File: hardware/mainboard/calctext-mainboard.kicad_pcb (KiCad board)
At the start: 4 copper layers, 65 x 97.8 mm, 9 parts, among them J1 Conn_ARM_SWD_TagConnect_TC203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

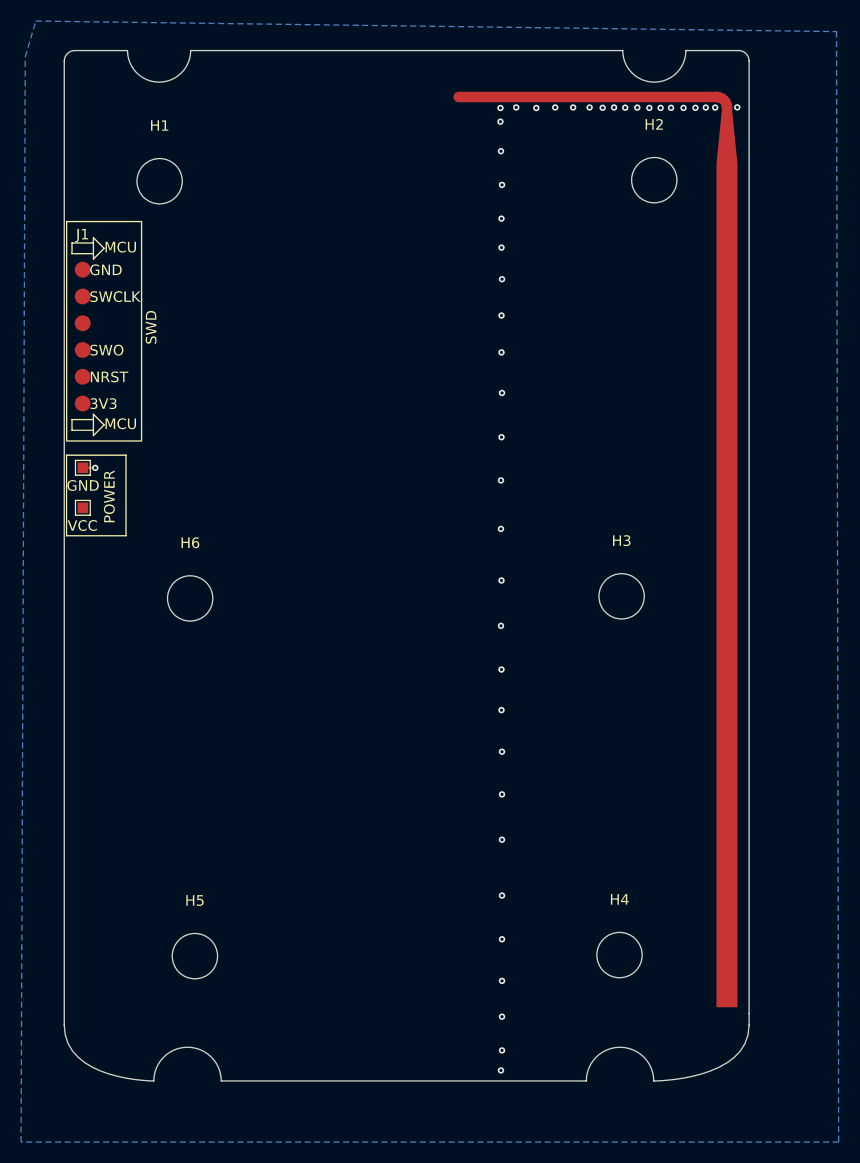
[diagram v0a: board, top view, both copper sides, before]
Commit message: Lay out calculator keypad contacts
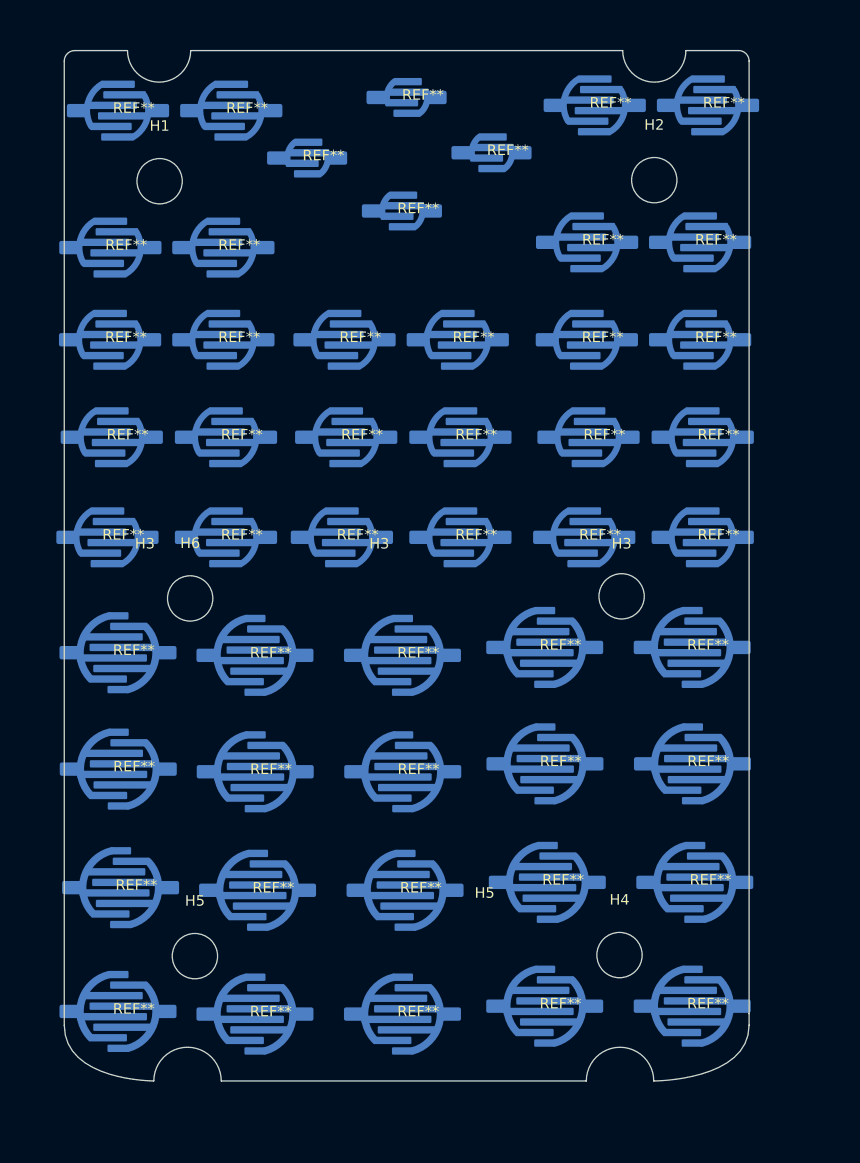
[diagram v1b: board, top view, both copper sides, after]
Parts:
- removed J1: Conn_ARM_SWD_TagConnect_TC2030-NL, STLINKV2:STLINKV2
- removed TP2: +4.2V, TestPoint:TestPoint_Pad_1.0x1.0mm
- removed TP3: GND, TestPoint:TestPoint_Pad_1.0x1.0mm
- added REF**: keypad_trace_button_medium, CalcText:keypad_trace_button_medium, F.Cu at (21.3, 35.5)
- added REF**: keypad_trace_button_medium, CalcText:keypad_trace_button_medium, F.Cu at (66.5, 44.2)
- added REF**: keypad_trace_button_large, CalcText:keypad_trace_button_large, F.Cu at (62.5, 107.5)
- added REF**: keypad_trace_button_small, CalcText:keypad_trace_button_small, F.Cu at (49.4, 21.2)
- added REF**: keypad_trace_button_small, CalcText:keypad_trace_button_small, F.Cu at (49.0, 32.0)
- added REF**: keypad_trace_button_medium, CalcText:keypad_trace_button_medium, F.Cu at (66.7, 53.5)
- added REF**: keypad_trace_button_large, CalcText:keypad_trace_button_large, F.Cu at (35.0, 108.2)
- added REF**: keypad_trace_button_medium, CalcText:keypad_trace_button_medium, F.Cu at (22.0, 22.5)
- added REF**: keypad_trace_button_medium, CalcText:keypad_trace_button_medium, F.Cu at (78.0, 22.0)
- added REF**: keypad_trace_button_large, CalcText:keypad_trace_button_large, F.Cu at (49.2, 96.5)
- added REF**: keypad_trace_button_large, CalcText:keypad_trace_button_large, F.Cu at (22.2, 96.2)
- added REF**: keypad_trace_button_large, CalcText:keypad_trace_button_large, F.Cu at (76.7, 95.8)
- added REF**: keypad_trace_button_large, CalcText:keypad_trace_button_large, F.Cu at (35.2, 96.5)
- added REF**: keypad_trace_button_medium, CalcText:keypad_trace_button_medium, F.Cu at (32.0, 35.5)
- added REF**: keypad_trace_button_large, CalcText:keypad_trace_button_large, F.Cu at (22.0, 74.0)
- added REF**: keypad_trace_button_medium, CalcText:keypad_trace_button_medium, F.Cu at (43.7, 53.5)
- added REF**: keypad_trace_button_medium, CalcText:keypad_trace_button_medium, F.Cu at (43.2, 63.0)
- added REF**: keypad_trace_button_large, CalcText:keypad_trace_button_large, F.Cu at (76.5, 84.5)
- added REF**: keypad_trace_button_large, CalcText:keypad_trace_button_large, F.Cu at (49.0, 85.2)
- added REF**: keypad_trace_button_large, CalcText:keypad_trace_button_large, F.Cu at (62.5, 84.5)
- added REF**: keypad_trace_button_large, CalcText:keypad_trace_button_large, F.Cu at (22.0, 108.0)
- added REF**: keypad_trace_button_medium, CalcText:keypad_trace_button_medium, F.Cu at (77.2, 44.2)
- added REF**: keypad_trace_button_medium, CalcText:keypad_trace_button_medium, F.Cu at (54.5, 53.5)
- added REF**: keypad_trace_button_medium, CalcText:keypad_trace_button_medium, F.Cu at (77.2, 35.0)
- added REF**: keypad_trace_button_medium, CalcText:keypad_trace_button_medium, F.Cu at (21.2, 44.2)
- added REF**: keypad_trace_button_large, CalcText:keypad_trace_button_large, F.Cu at (76.5, 73.5)
- added REF**: keypad_trace_button_medium, CalcText:keypad_trace_button_medium, F.Cu at (43.5, 44.2)
- added REF**: keypad_trace_button_medium, CalcText:keypad_trace_button_medium, F.Cu at (54.5, 63.0)
- added REF**: keypad_trace_button_medium, CalcText:keypad_trace_button_medium, F.Cu at (77.5, 53.5)
- added REF**: keypad_trace_button_medium, CalcText:keypad_trace_button_medium, F.Cu at (66.2, 63.0)
- added REF**: keypad_trace_button_large, CalcText:keypad_trace_button_large, F.Cu at (35.0, 74.2)
- added REF**: keypad_trace_button_large, CalcText:keypad_trace_button_large, F.Cu at (62.7, 95.8)
- added REF**: keypad_trace_button_medium, CalcText:keypad_trace_button_medium, F.Cu at (67.2, 22.0)
- added REF**: keypad_trace_button_medium, CalcText:keypad_trace_button_medium, F.Cu at (54.2, 44.2)
- added REF**: keypad_trace_button_medium, CalcText:keypad_trace_button_medium, F.Cu at (21.0, 63.0)
- added REF**: keypad_trace_button_medium, CalcText:keypad_trace_button_medium, F.Cu at (21.4, 53.5)
- added REF**: keypad_trace_button_small, CalcText:keypad_trace_button_small, F.Cu at (40.0, 27.0)
- added REF**: keypad_trace_button_large, CalcText:keypad_trace_button_large, F.Cu at (22.0, 85.0)
- added REF**: keypad_trace_button_medium, CalcText:keypad_trace_button_medium, F.Cu at (77.5, 63.0)
- added REF**: keypad_trace_button_medium, CalcText:keypad_trace_button_medium, F.Cu at (32.2, 63.0)
- added REF**: keypad_trace_button_medium, CalcText:keypad_trace_button_medium, F.Cu at (66.5, 35.0)
- added REF**: keypad_trace_button_large, CalcText:keypad_trace_button_large, F.Cu at (62.5, 73.5)
- added REF**: keypad_trace_button_medium, CalcText:keypad_trace_button_medium, F.Cu at (32.8, 22.5)
- added REF**: keypad_trace_button_large, CalcText:keypad_trace_button_large, F.Cu at (49.0, 108.2)
- added REF**: keypad_trace_button_large, CalcText:keypad_trace_button_large, F.Cu at (76.5, 107.5)
- added REF**: keypad_trace_button_medium, CalcText:keypad_trace_button_medium, F.Cu at (32.0, 44.2)
- added REF**: keypad_trace_button_large, CalcText:keypad_trace_button_large, F.Cu at (49.0, 74.2)
- added REF**: keypad_trace_button_large, CalcText:keypad_trace_button_large, F.Cu at (35.0, 85.2)
- added REF**: keypad_trace_button_medium, CalcText:keypad_trace_button_medium, F.Cu at (32.2, 53.5)
- added REF**: keypad_trace_button_small, CalcText:keypad_trace_button_small, F.Cu at (57.5, 26.5)
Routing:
- net (no net): track 26.3 -> 0.00 mm
- net GND: track 1.18 -> 0.00 mm, vias 44 -> 0
- removed copper zone on B.Cu, net GND
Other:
- board text added: "H3"
- board text added: "H5"
- board text removed: "GND"
- board text removed: "POWER"
- board text removed: "VCC"

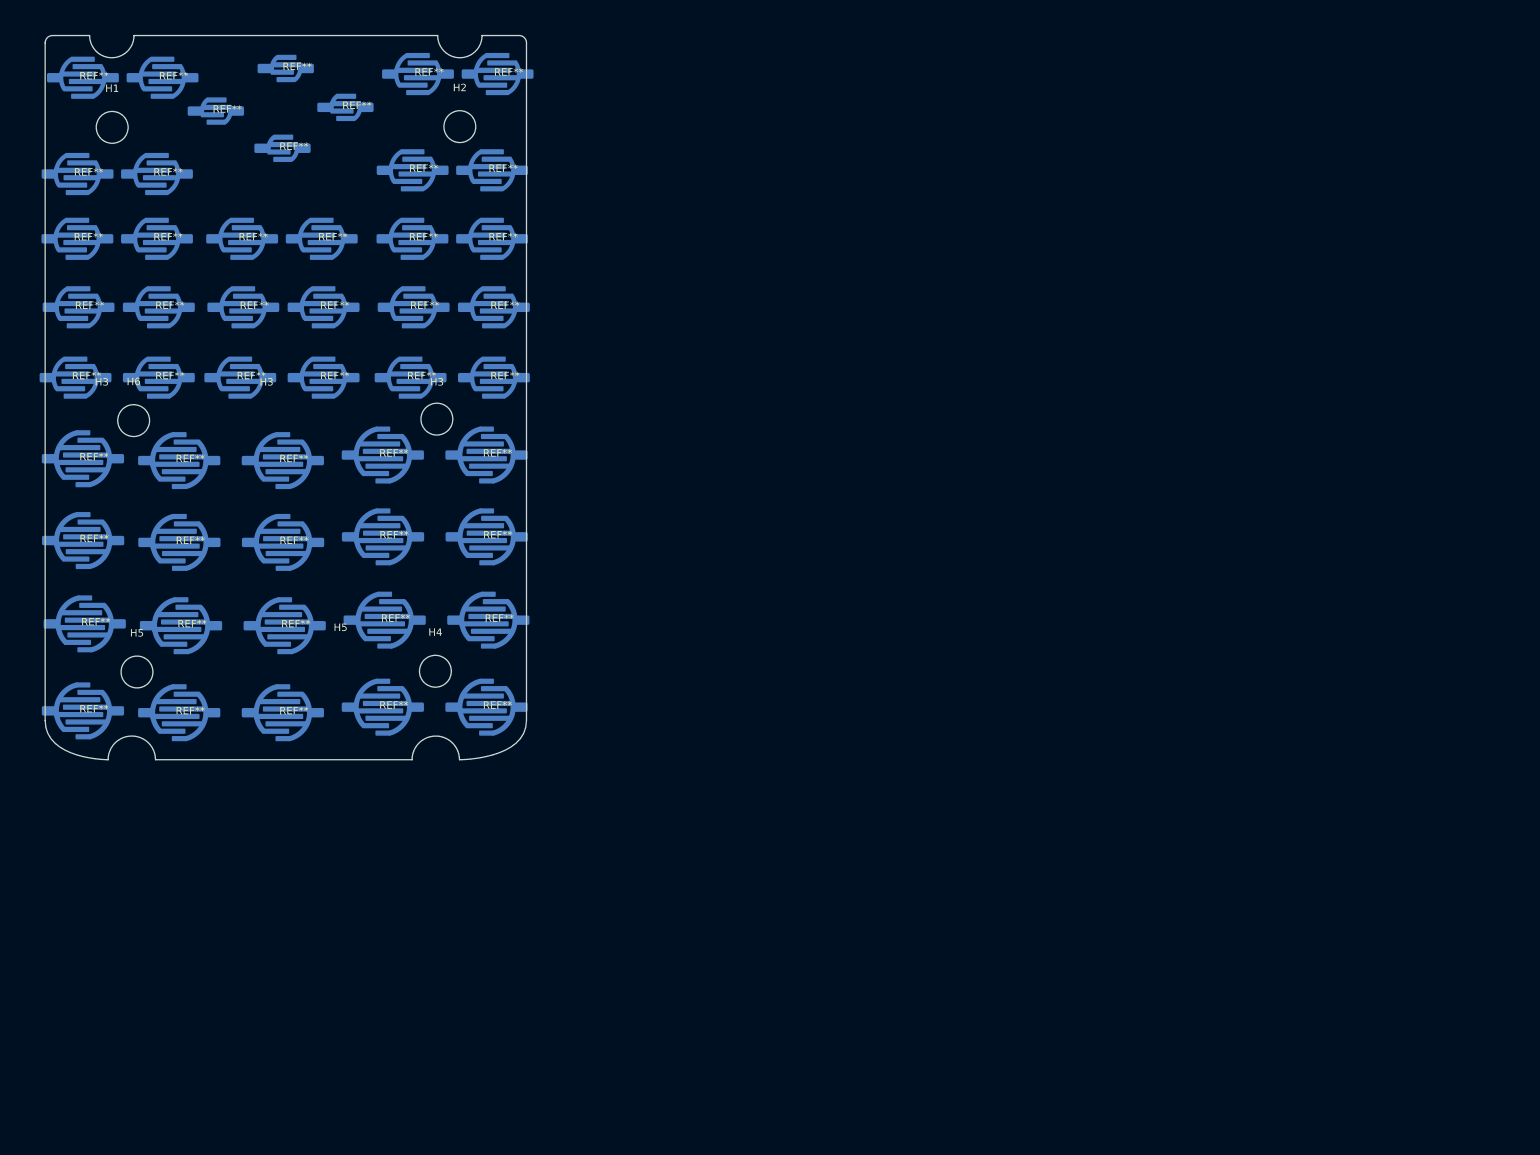
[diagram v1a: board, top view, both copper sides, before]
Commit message: Refine keypad contacts and mechanical alignment
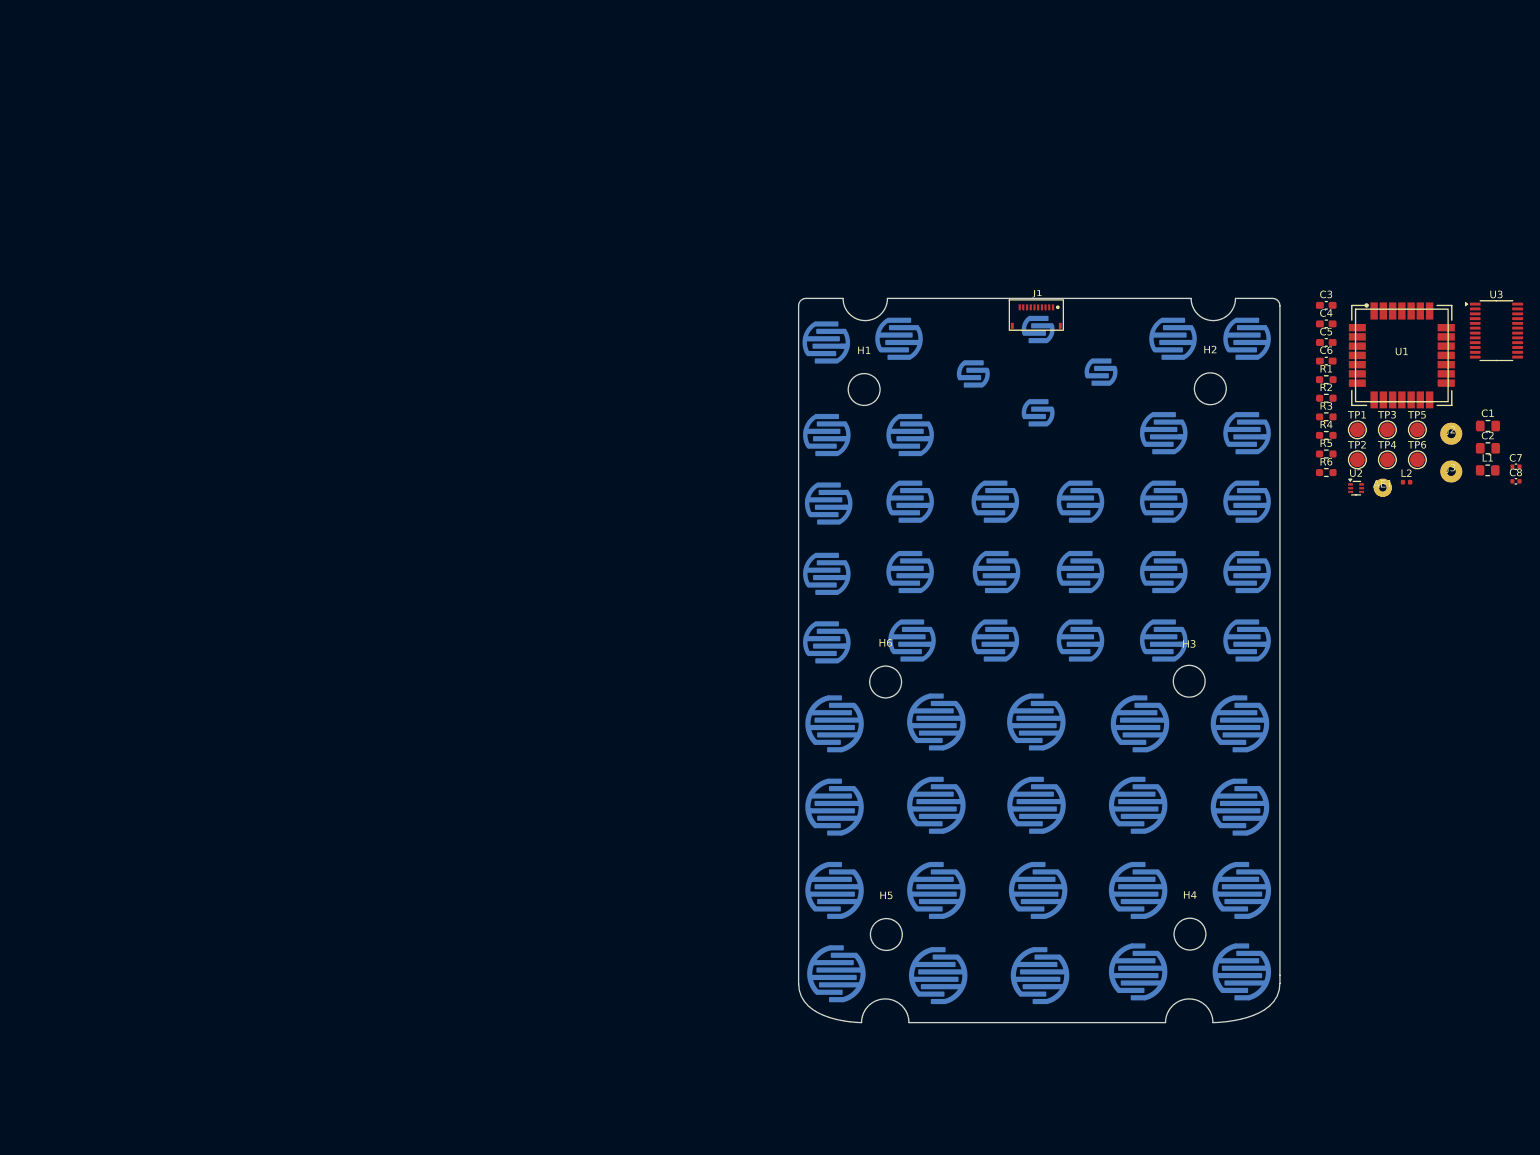
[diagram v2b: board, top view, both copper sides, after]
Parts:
- added AE1: Antenna, CalcText:Wire_Antenna_PTH, F.Cu at (197.5, 77.9)
- added C1: 10uF, Capacitor_SMD:C_0805_2012Metric_Pad1.18x1.45mm_HandSolder, F.Cu at (211.7, 69.5)
- added C2: 10uF, Capacitor_SMD:C_0805_2012Metric_Pad1.18x1.45mm_HandSolder, F.Cu at (211.7, 72.5)
- added C3: 100nF, Capacitor_SMD:C_0603_1608Metric_Pad1.08x0.95mm_HandSolder, F.Cu at (189.9, 53.2)
- added C4: 4.7uF, Capacitor_SMD:C_0603_1608Metric_Pad1.08x0.95mm_HandSolder, F.Cu at (189.9, 55.7)
- added C5: 100nF, Capacitor_SMD:C_0603_1608Metric_Pad1.08x0.95mm_HandSolder, F.Cu at (189.9, 58.2)
- added C6: 100nF, Capacitor_SMD:C_0603_1608Metric_Pad1.08x0.95mm_HandSolder, F.Cu at (189.9, 60.8)
- added C7: DNP, Capacitor_SMD:C_0402_1005Metric, F.Cu at (215.5, 75.0)
- added C8: DNP, Capacitor_SMD:C_0402_1005Metric, F.Cu at (215.5, 77.0)
- added J1: LCD_FFC, CalcText_Shared:Hirose_FH34SRJ-10S-0.5SH, F.Cu at (150.8, 53.5)
- added J2: J_BAT+, CalcText:Wire_Solder_PTH, F.Cu at (206.8, 70.6)
- added J3: J_BAT-, CalcText:Wire_Solder_PTH, F.Cu at (206.8, 75.7)
- added L1: 1uH, Inductor_SMD:L_0805_2012Metric_Pad1.15x1.40mm_HandSolder, F.Cu at (211.7, 75.5)
- added L2: 0R, Inductor_SMD:L_0402_1005Metric, F.Cu at (200.8, 77.1)
- added R1: 100kΩ, Resistor_SMD:R_0603_1608Metric_Pad0.98x0.95mm_HandSolder, F.Cu at (189.9, 63.3)
- added R2: 100kΩ, Resistor_SMD:R_0603_1608Metric_Pad0.98x0.95mm_HandSolder, F.Cu at (189.9, 65.8)
- added R3: 100kΩ, Resistor_SMD:R_0603_1608Metric_Pad0.98x0.95mm_HandSolder, F.Cu at (189.9, 68.3)
- added R4: 10kΩ, Resistor_SMD:R_0603_1608Metric_Pad0.98x0.95mm_HandSolder, F.Cu at (189.9, 70.8)
- added R5: 10kΩ, Resistor_SMD:R_0603_1608Metric_Pad0.98x0.95mm_HandSolder, F.Cu at (189.9, 73.3)
- added R6: 10kΩ, Resistor_SMD:R_0603_1608Metric_Pad0.98x0.95mm_HandSolder, F.Cu at (189.9, 75.8)
- added TP1: SWDIO, TestPoint:TestPoint_Pad_D2.0mm, F.Cu at (194.1, 70.0)
- added TP2: SWDCLK, TestPoint:TestPoint_Pad_D2.0mm, F.Cu at (194.1, 74.1)
- added TP3: NRST, TestPoint:TestPoint_Pad_D2.0mm, F.Cu at (198.2, 70.0)
- added TP4: SWO, TestPoint:TestPoint_Pad_D2.0mm, F.Cu at (198.2, 74.1)
- added TP5: 3V3, TestPoint:TestPoint_Pad_D2.0mm, F.Cu at (202.2, 70.0)
- added TP6: GND, TestPoint:TestPoint_Pad_D2.0mm, F.Cu at (202.2, 74.1)
- added U1: Wio-E5-LE, CalcText:Wio-E5-LE, F.Cu at (200.1, 60.0)
- added U2: TPS61299, Package_TO_SOT_SMD:Texas_R-PDSO-N6_DRL-6, F.Cu at (193.9, 77.9)
- added U3: PCAL9535APW,118, Package_SO:TSSOP-24_4.4x7.8mm_P0.65mm, F.Cu at (212.9, 56.6)
- SW1: renamed from REF**; value keypad_trace_button_medium -> Keypad_Contact
- moved REF** 108.5 mm to (164.8, 109.8)
- moved REF** 108.5 mm to (137.5, 143.8)
- moved REF** 108.5 mm to (156.8, 79.8)
- moved REF** 108.3 mm to (156.8, 89.2)
- moved REF** 108.2 mm to (156.8, 98.5)
- moved REF** 108.2 mm to (142.2, 62.5)
- moved REF** 108.2 mm to (151.2, 143.8)
- moved REF** 108.2 mm to (164.5, 120.8)
- moved REF** 108.2 mm to (137.2, 120.8)
- moved REF** 108.2 mm to (137.2, 109.5)
- moved REF** 108.1 mm to (178.5, 132.2)
- moved REF** 108.1 mm to (164.5, 132.2)
- moved REF** 108.1 mm to (137.2, 132.2)
- moved REF** 108.1 mm to (164.5, 143.2)
- moved REF** 108.1 mm to (169.2, 57.8)
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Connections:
- SW1 pad 1: (no net) -> 3V3
- SW1 pad 2: (no net) -> WAKEUP_PIN
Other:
- outline, holes or cut-outs redrawn
